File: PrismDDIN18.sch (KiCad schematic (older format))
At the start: 89 parts, among them CON1 BARREL_JACK, IC1 LM2596T-5, J1 Conn_01x03, M1 IN-18, M10 IN-18, Q2 2N7000, Q3 2N7000, Q4 2N7000, Q5 2N7000, Q6 IRF640, Q7 2N3906, U1 WeMos_mini, U2 MC34063A, U3 HV5622, U4 HV5622, U5 DS1307+, Y1 32.768kHz

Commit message: correct LV inductor value
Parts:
- L2: footprint NixieClockMaster:Inductor-33mH-TH-SMD -> NixieClockMaster:Inductor-100mH
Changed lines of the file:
@@
 F 0 "L2" V 9400 9350 70  0000 L BNN
 F 1 "100uH" V 9600 9200 70  0000 L BNN
-F 2 "NixieClockMaster:Inductor-33mH-TH-SMD" H 9440 9190 70  0001 L TNN
+F 2 "NixieClockMaster:Inductor-100mH" H 9440 9190 70  0001 L TNN
 F 3 "" H 9450 9400 60  0001 C CNN
 	1    9450 9400

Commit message: Contribution from Hartmut with sk6812 mini
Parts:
- removed LED1, LED2, LED3, LED4, LED5, LED6: WS2812B, NixieClockMaster:WS2812B, symbol PrismDDIN18-rescue:WS2812B
- removed U5: DS1307+, NixieClockMaster:DS1307_DIL8, symbol Timer_RTC:DS1307+
- added LED1, LED2, LED3, LED4, LED5, LED6: SK6812MINI, LED_SMD:LED_SK6812MINI_PLCC4_3.5x3.5mm_P1.75mm, symbol PrismDDIN18-rescue:SK6812MINI-LED1
- added U5: DS1307+DIL8, Package_DIP:DIP-8_W7.62mm, symbol PrismDDIN18-rescue:DS1307+DIL8-Timer_RTC
- L2: footprint NixieClockMaster:Inductor-100mH -> NixieClockMaster:Inductor-33mH-TH-SMD
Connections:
- wire segments 498 -> 504
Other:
- moved on the sheet: C1, C2, C3, C4, C5, C6, Y1

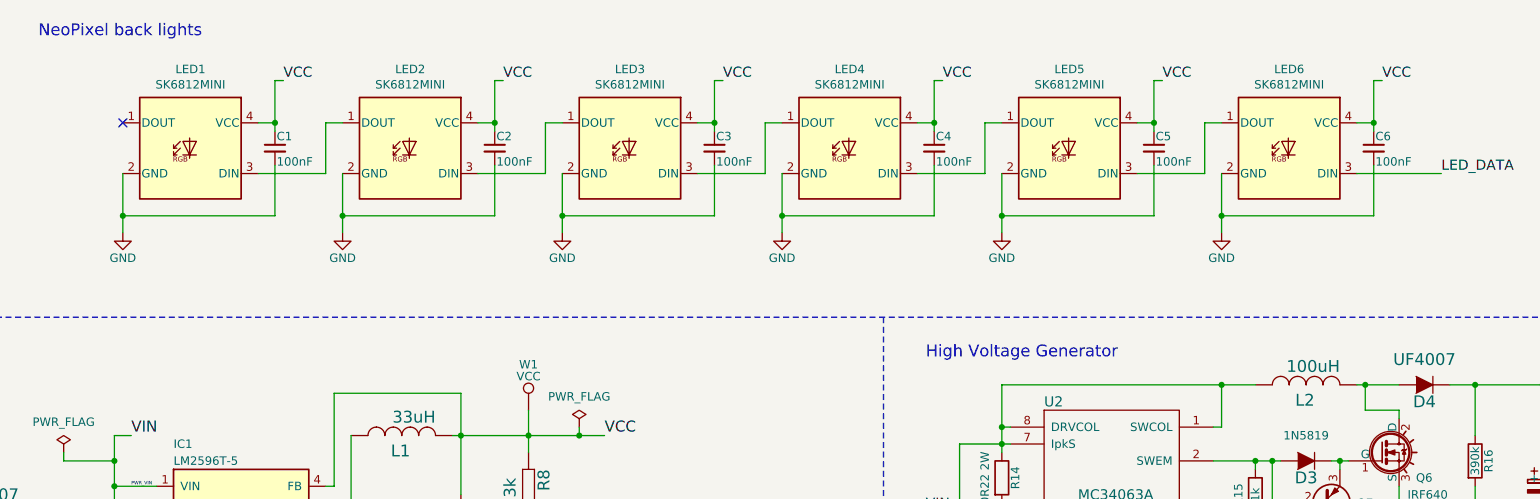
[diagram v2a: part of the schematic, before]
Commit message: Use APA106
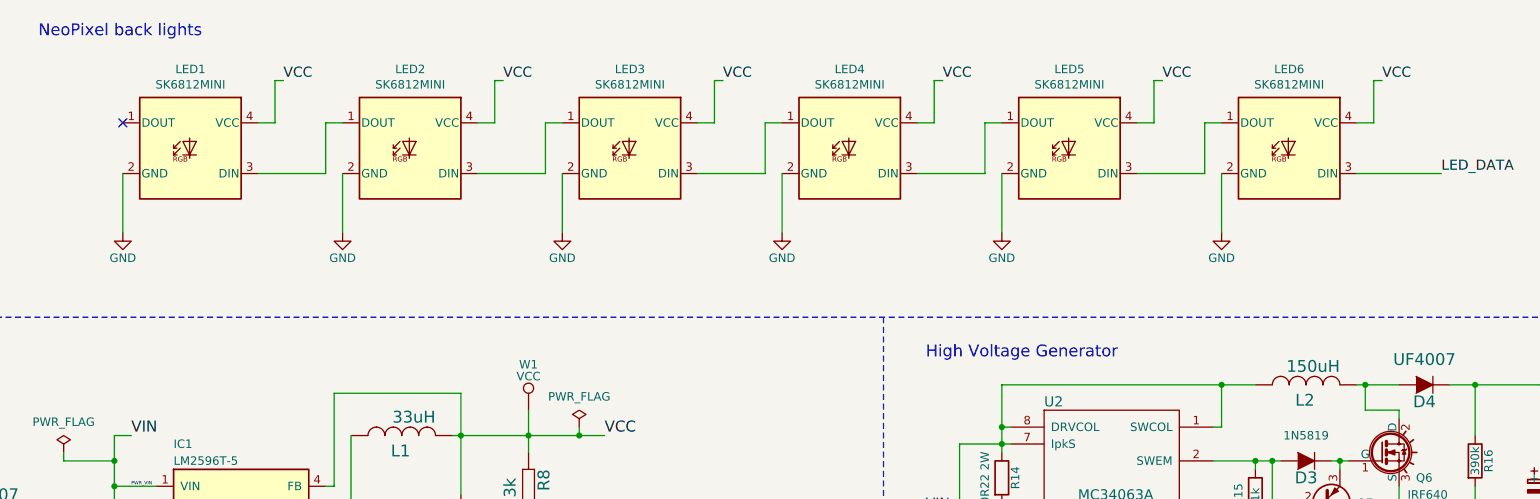
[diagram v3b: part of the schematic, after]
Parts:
- removed C1, C2, C3, C4, C5, C6: 100nF, NixieClockMaster:C025-024X044, symbol PrismDDIN18-rescue:C_Small
- H1, H10, M1, M10, S1, S10: footprint NixieClockMaster:IN-18 -> NixieClockMaster:nixies-us-IN-18
- L2: value 100uH -> 150uH
- LED1, LED2, LED3, LED4, LED5, LED6: footprint LED_SMD:LED_SK6812MINI_PLCC4_3.5x3.5mm_P1.75mm -> NixieClockMaster:LED5_RGB_CA_Offset_Tighter
- R14: footprint NixieClockMaster:R-0207_2V -> NixieClockMaster:R_2W
- R18, R19, R2, R3, R4, R5, R6: footprint NixieClockMaster:R-0207_2V -> NixieClockMaster:R_Short_P7.62mm_Horizontal
- U5: footprint Package_DIP:DIP-8_W7.62mm -> NixieClockMaster:DS1307_DIL8

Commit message: fAB
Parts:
- removed C17: 220uF 35V, NixieClockMaster:C_Radial_D6.3_L11.2_P2.5, symbol PrismDDIN18-rescue:CP
- removed C18: 680pF, NixieClockMaster:C025-024X044, symbol PrismDDIN18-rescue:C
- removed C19: 100nF, NixieClockMaster:C025-024X044, symbol PrismDDIN18-rescue:C
- removed C20: 2.2uF 400V, NixieClockMaster:C_Radial_D6.3_L11.2_P2.5, symbol PrismDDIN18-rescue:CP
- removed D3: 1N5819, NixieClockMaster:Diode_DO-41_1N4001, symbol PrismDDIN18-rescue:D-RESCUE-KickstarterNixie
- removed D4: UF4007, NixieClockMaster:Diode_DO-41_1N4001, symbol PrismDDIN18-rescue:D-RESCUE-KickstarterNixie
- removed L2: 150uH, NixieClockMaster:Inductor-33mH-TH-SMD, symbol PrismDDIN18-rescue:RCL_L-US6000-XXX-RC
- removed Q6: IRF640, NixieClockMaster:TO-220-3_H, symbol PrismDDIN18-rescue:IRF540N-RESCUE-DDIN18
- removed Q7: 2N3906, NixieClockMaster:2N7000_TO92, symbol Device:Q_PNP_CBE
- removed R14: 0R22 2W, NixieClockMaster:R_2W, symbol PrismDDIN18-rescue:R
- removed R15: 1k, NixieClockMaster:R-0207_2V, symbol PrismDDIN18-rescue:R
- removed R16: 390k, NixieClockMaster:R-0207_2V, symbol PrismDDIN18-rescue:R
- removed R17: 2k2, NixieClockMaster:R-0207_2V, symbol PrismDDIN18-rescue:R
- removed RV1: 5k, NixieClockMaster:Potentiometer_Trimmer_Bourns_3296X, symbol PrismDDIN18-rescue:POT
- removed U2: MC34063A, NixieClockMaster:MC34063_DIL8, symbol PrismDDIN18-rescue:MC34063A
- added JP1: SolderJumper_3_Open, NixieClockMaster:SOLDER-JUMPER_2-WAY, symbol Jumper:SolderJumper_3_Open
- added U2: HVSMPS-34063, NixieClockMaster:HVSMPS-34063, symbol NixieClockMaster:HVSMPS-34063
- LED1, LED2, LED3, LED4, LED5, LED6: footprint NixieClockMaster:LED5_RGB_CA_Offset_Tighter -> LED_SMD:LED_SK6812MINI_PLCC4_3.5x3.5mm_P1.75mm
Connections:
- net GND: now also U2.2 (GND), U2.3 (GND)
- net HV: now also U2.4 (HV)
- net PWR_VIN: now also JP1.1 (A), U2.1 (VIN)
- net VCC: now also JP1.3 (B); no longer R11.1, R13.1, R23.1, R24.1, U3.22 (POL), U3.25 (VCC), U4.22 (POL), U4.25 (VCC)
- new net VSup: JP1.2 (C), R11.1, R13.1, R23.1, R24.1, U3.22 (POL), U3.25 (VCC), U4.22 (POL), U4.25 (VCC)
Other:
- moved on the sheet: J1, W3

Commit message: Update to new layout
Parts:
- removed H1, H10, M1, M10, S1, S10: IN-18, NixieClockMaster:nixies-us-IN-18, symbol PrismDDIN18-rescue:IN-18
- removed JP1: SolderJumper_3_Open, NixieClockMaster:SOLDER-JUMPER_2-WAY, symbol Jumper:SolderJumper_3_Open
- removed LED1, LED2, LED3, LED4, LED5, LED6: SK6812MINI, LED_SMD:LED_SK6812MINI_PLCC4_3.5x3.5mm_P1.75mm, symbol PrismDDIN18-rescue:SK6812MINI-LED1
- removed Q2, Q3, Q4, Q5: 2N7000, NixieClockMaster:TO-92_inline_2N7000, symbol Transistor_FET:2N7000
- removed R10, R11, R12, R13, R22, R23, R24, R7: 10k, NixieClockMaster:R-0207_2V, symbol Device:R
- added C1, C2, C3, C4, C5, C6: 100nF, Capacitor_SMD:C_1206_3216Metric, symbol PrismDDIN18-rescue:C_Small
- added C17: 220uF 35V, NixieClockMaster:C_Radial_D6.3_L11.2_P2.5, symbol PrismDDIN18-rescue:CP
- added C9: 100nF, NixieClockMaster:C025-024X044, symbol Device:C
- added H1, H10, M1, M10, S1, S10: Z566M, NixieClockMaster:IN-18-standoff-pins, symbol PrismDDIN18-rescue:Z566M
- added J2: EXT_LED_OUT, NixieClockMaster:Header_MA03-1_Small, symbol Connector_Generic:Conn_01x03
- added LED1, LED2, LED3, LED4, LED5, LED6: WS2812B_3535, NixieClockMaster:WS2812B-SmallPads, symbol PrismDDIN18-rescue:WS2812B_3535-LED1-PrismDDZ566M-rescue
- added MH1, MH2, MH3, MH4, MH5, MH6: MountingHole, NixieClockMaster:MountingHole_3.2mm_M3, symbol Mechanical:MountingHole
- added R7: R_PHOTO, NixieClockMaster:C_Naked, symbol Device:R_PHOTO
- added SW1: SW_Push, Button_Switch_SMD:SW_SPST_CK_RS282G05A3, symbol PrismDDIN18-rescue:SW_Push-Switch-PrismDDZ566M-rescue
- added U6: CD40109, Package_DIP:DIP-16_W7.62mm, symbol NixieClockMaster:CD40109
- added W5: VIN, NixieClockMaster:TESTPAD_P1-13, symbol PrismDDIN18-rescue:TEST_1P
- BT1: symbol Device:Battery_Cell -> PrismDDIN18-rescue:Battery_Cell-Device-PrismDDZ566M-rescue
- C21, C7: symbol Device:C -> PrismDDIN18-rescue:C-Device-PrismDDZ566M-rescue
- C8: value 220uF -> 220uF 10V; symbol Device:CP -> PrismDDIN18-rescue:CP-Device-PrismDDZ566M-rescue
- IC1: footprint NixieClockMaster:TO220-5A -> NixieClockMaster:TO220-5A_H
- J1: value Conn_01x03 -> LED_TEST
- R18, R19: value 10k -> 120k
- R20: renamed from R21; value 10k -> 120k; footprint NixieClockMaster:R-0207_2V -> NixieClockMaster:R_Short_P7.62mm_Horizontal
- R21: renamed from R20; value 10k -> 120k; footprint NixieClockMaster:R-0207_2V -> NixieClockMaster:R_Short_P7.62mm_Horizontal
- U1: footprint NixieClockMaster:WeMos_D1_mini_board_flipped -> NixieClockMaster:WeMos_D1_mini_board_simple
- U5: footprint NixieClockMaster:DS1307_DIL8 -> Package_DIP:DIP-8_W7.62mm; symbol PrismDDIN18-rescue:DS1307+DIL8-Timer_RTC -> PrismDDIN18-rescue:DS1307+DIL8-Timer_RTC-PrismDDZ566M-rescue
- Y1: symbol Device:Crystal_Small -> PrismDDIN18-rescue:Crystal_Small-Device-PrismDDZ566M-rescue
- renumbered D6 to D5, D5 to D6, D8 to D7, D7 to D8
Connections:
- net VSup is gone; now on net PWR_VIN: U3.22 (POL), U3.25 (VCC), U4.22 (POL), U4.25 (VCC)
- net 3V3: now also U6.1 (VCCA), U6.15 (EN4), U6.2 (EN1), U6.7 (EN2), U6.9 (EN3)
- net BLANK: now also U6.5 (OUT2)
- net BLANK_3V3: now also U6.6 (IN2)
- net BTN1: now also SW1.2
- net CLK: now also U6.11 (OUT3)
- net CLK_3V3: now also U6.10 (IN3)
- net DATA1: now also U6.4 (OUT1)
- net DATA1_3V3: now also U6.3 (IN1)
- net DLS: now also R7.1
- net GND: now also C1.2, C17.2, C2.2, C3.2, C4.2, C5.2, C6.2, C9.2, J2.2 (Pin_2), LED1.3 (GND), LED2.3 (GND), LED3.3 (GND), LED4.3 (GND), LED5.3 (GND), LED6.3 (GND), R7.2, SW1.1, U6.8 (GND)
- net H10_0: now also H10.0
- net H10_1: now also H10.1
- net H10_2: now also H10.2
- net H10_3: now also H10.3
- net H10_4: now also H10.4
- net H10_5: now also H10.5
- net H10_6: now also H10.6
- net H10_7: now also H10.7
- net H10_8: now also H10.8
- net H10_9: now also H10.9
- net H1_0: now also H1.0
- net H1_1: now also H1.1
- net H1_2: now also H1.2
- net H1_3: now also H1.3
- net H1_4: now also H1.4
- net H1_5: now also H1.5
- net H1_6: now also H1.6
- net H1_7: now also H1.7
- net H1_8: now also H1.8
- net H1_9: now also H1.9
- net LATCH: now also U6.13 (OUT4)
- net LATCH_3V3: now also U6.14 (IN4)
- net LED_DATA: now also LED6.4 (DIN)
- net M10_0: now also M10.0
- net M10_1: now also M10.1
- net M10_2: now also M10.2
- net M10_3: now also M10.3
- net M10_4: now also M10.4
- net M10_5: now also M10.5
- net M10_6: now also M10.6
- net M10_7: now also M10.7
- net M10_8: now also M10.8
- net M10_9: now also M10.9
- net M1_0: now also M1.0
- net M1_1: now also M1.1
- net M1_2: now also M1.2
- net M1_3: now also M1.3
- net M1_4: now also M1.4
- net M1_5: now also M1.5
- net M1_6: now also M1.6
- net M1_7: now also M1.7
- net M1_8: now also M1.8
- net M1_9: now also M1.9
- net PWR_VIN: now also C17.1, C9.1, U6.16 (VCCB), W5.1
- net S10_0: now also S10.0
- net S10_1: now also S10.1
- net S10_2: now also S10.2
- net S10_3: now also S10.3
- net S10_4: now also S10.4
- net S10_5: now also S10.5
- net S10_6: now also S10.6
- net S10_7: now also S10.7
- net S10_8: now also S10.8
- net S10_9: now also S10.9
- net S1_0: now also S1.0
- net S1_1: now also S1.1
- net S1_2: now also S1.2
- net S1_3: now also S1.3
- net S1_4: now also S1.4
- net S1_5: now also S1.5
- net S1_6: now also S1.6
- net S1_7: now also S1.7
- net S1_8: now also S1.8
- net S1_9: now also S1.9
- net VCC: now also C1.1, C2.1, C3.1, C4.1, C5.1, C6.1, J2.3 (Pin_3), LED1.1 (VCC), LED2.1 (VCC), LED3.1 (VCC), LED4.1 (VCC), LED5.1 (VCC), LED6.1 (VCC)
- net at R5.2: now also S10.A
- net at R4.2: now also M1.A
- net at R2.2: now also H1.A
- net at R3.2: now also M10.A
- net at R6.2: now also S1.A
- net at R1.2: now also H10.A
- new net: J2.1 (Pin_1), LED1.2 (DOUT)
- new net: LED1.4 (DIN), LED2.2 (DOUT)
- new net: LED2.4 (DIN), LED3.2 (DOUT)
- new net: LED5.4 (DIN), LED6.2 (DOUT)
- new net: LED4.4 (DIN), LED5.2 (DOUT)
- new net: LED3.4 (DIN), LED4.2 (DOUT)
- no-connect marks 12 -> 5
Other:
- note added: "Level shifter"
- note removed: "Level shifters"
- moved on the sheet: CON1, J1, R9, SV4, W3

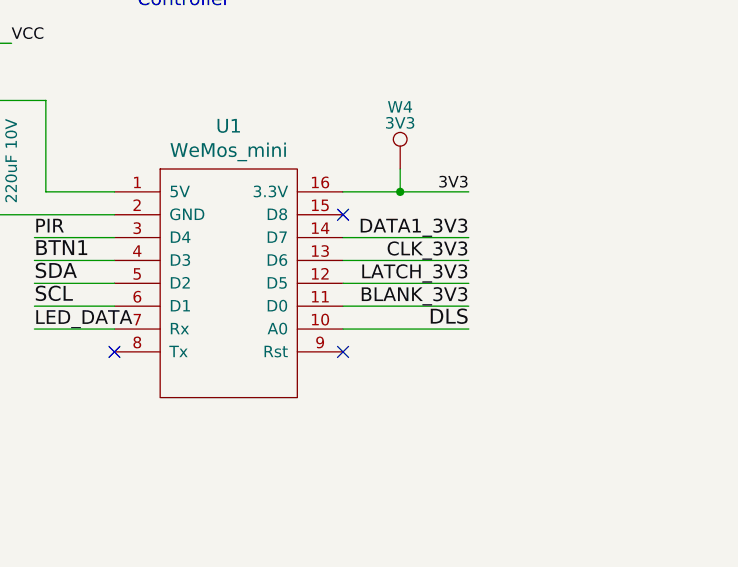
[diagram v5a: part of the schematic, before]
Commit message: Change pin size of socket, swap D0 and D5 for PWM blanking
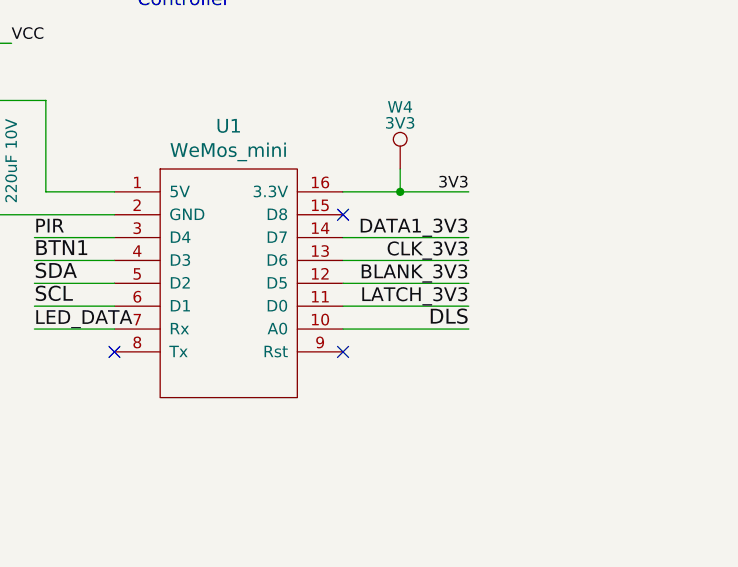
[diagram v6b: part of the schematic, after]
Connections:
- net BLANK_3V3: now also U1.12 (D5); no longer U1.11 (D0)
- net LATCH_3V3: now also U1.11 (D0); no longer U1.12 (D5)
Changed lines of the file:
@@
 Text Label 14950 8500 2    60   ~ 0
 CLK_3V3
+Text Label 14950 8700 2    60   ~ 0
+LATCH_3V3
 Text Label 14950 8600 2    60   ~ 0
-LATCH_3V3
-Text Label 14950 8700 2    60   ~ 0
 BLANK_3V3
 Wire Wire Line
